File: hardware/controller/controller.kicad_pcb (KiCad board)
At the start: 4 copper layers, 100 x 70 mm, 208 parts, among them J1 USB_C_Receptacle_USB2.0_14P, J10 Conn_01x01, J11 Conn_01x01, J12 Conn_01x09, J13 Mini-SPOX, J14 Mini-SPOX, J2 IDC-10, J3 XT-60, J4 Conn_01x07, J5 Conn_01x01, J6 Conn_01x01, J7 Conn_01x01, J8 Conn_01x09, J9 Conn_01x01, Q1 DMPH4013SK3, Q10 IPD90N04S4L04, Q11 IPD90N04S4L04, Q12 IPD90N04S4L04, Q13 IPD90N04S4L04, Q2 IPD90N04S4L04, Q3 IPD90N04S4L04, Q4 IPD90N04S4L04, Q5 IPD90N04S4L04, Q6 IPD90N04S4L04, Q7 IPD90N04S4L04, Q8 IPD90N04S4L04, Q9 IPD90N04S4L04, SW1 SW_Push, SW2 SW_SPST, U1 USBLC6-2SC6, U10 MCP6541, U11 LM2105D, U12 MCP6541, U13 LM2105D, U14 MCP6541, U15 LM2105D, U16 MCP6541, U17 LM2105D, U18 MCP6541, U19 LM2105D, U2 STM32H523RETx, U20 TXS0101DBV, U21 TXS0101DBV, U3 ESP32-C3-WROOM-02, U4 LM1117MP-3.3, U5 LV14340, U6 MPU-6050, U7 HMC5883L, U8 MCP6541, U9 LM2105D, Y1 8MHz

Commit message: wip
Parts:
- R14, R16: moved to F.Cu
- moved R20 14.7 mm to (156.0, 59.6)
- moved R2 13.4 mm to (108.8, 59.4), turned to -90 degrees
- moved R18 11.8 mm to (192.2, 63.4)
- moved C35 11.5 mm to (191.4, 68.0), turned to -90 degrees
- moved R19 11.2 mm to (192.2, 65.4), turned to 180 degrees
- moved C30 11.0 mm to (182.0, 63.8)
- moved C31 8.32 mm to (186.4, 70.4), turned to 0 degrees
- moved C33 5.74 mm to (175.6, 66.0), turned to 0 degrees
- moved C32 5.47 mm to (176.4, 63.6), turned to 0 degrees
- moved R17 5.47 mm to (170.6, 63.4)
- moved D4 5.47 mm to (170.6, 65.4)
- moved R16 5.34 mm to (160.0, 90.8)
- moved R14 5.26 mm to (163.4, 90.8)
- moved C18 2.76 mm to (158.2, 62.2), turned to 90 degrees
- moved C37 2.30 mm to (152.8, 53.2)
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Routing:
- net SERVO2_DATA: track 4.53 -> 114.6 mm
- net Net-(SW2-A): track 0.00 -> 80.4 mm, vias 0 -> 1
- net +5V: track 15.8 -> 86.2 mm, vias 1 -> 4
- net SERVO1_DATA: track 10.8 -> 63.4 mm
- net GND: track 177.8 -> 213.5 mm, vias 240 -> 258
- net +3.3V: track 163.1 -> 193.4 mm, vias 22 -> 35
- net IMU_SDA: track 28.8 -> 50.7 mm, vias 2 -> 4
- net IMU_SCL: track 29.5 -> 49.5 mm, vias 2 -> 4
- net /microcontroller/STM_RESET: track 16.4 -> 29.7 mm
- net MAG_SCL: track 15.8 -> 26.1 mm
- net IMU_INT: track 24.4 -> 33.1 mm
- net /microcontroller/ESP_USB_CC2: track 6.47 -> 13.2 mm
- net MAG_SDA: track 14.8 -> 21.1 mm
- net /sensors/MAG_C1: track 0.00 -> 6.12 mm
- net Net-(Q1-G): track 0.00 -> 5.65 mm, vias 0 -> 1
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
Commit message: wip - ready, but need double check
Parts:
- moved G*** 85.3 mm to (150.0, 80.7)
- moved G*** 72.5 mm to (145.2, 71.8)
- moved G*** 72.5 mm to (154.2, 71.8)
- moved C73 6.88 mm to (166.5, 109.2), turned to -90 degrees
- moved C69 6.64 mm to (137.5, 109.2), turned to -90 degrees
- moved C70 5.46 mm to (132.8, 105.8), turned to 90 degrees
- moved C74 4.85 mm to (161.0, 106.2), turned to 180 degrees
- moved R15 0.87 mm to (148.0, 89.2), turned to 0 degrees
- moved D4 0.81 mm to (169.8, 65.4)
- moved R17 0.81 mm to (169.8, 63.4)
- moved R14 0.80 mm to (163.4, 91.6)
- moved R16 0.80 mm to (160.0, 91.6)
- moved U20 0.56 mm to (134.0, 109.5), turned to 180 degrees
- moved U21 0.56 mm to (163.0, 109.5), turned to 180 degrees
- moved C72 0.25 mm to (136.8, 109.5)
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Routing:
- net +3.3V: track 193.4 -> 296.3 mm, vias 35 -> 45
- net +5V: track 86.2 -> 164.0 mm, vias 4 -> 7
- net GND: track 213.5 -> 265.9 mm, vias 258 -> 300
- net SERVO1_DATA: track 63.4 -> 88.5 mm
- net VBUS: track 78.5 -> 99.8 mm
- net Net-(U5-FB): track 0.00 -> 11.8 mm, vias 0 -> 1
- net Net-(U5-SS): track 0.00 -> 5.17 mm
- net SERVO2_DATA: track 114.6 -> 109.7 mm
- net Net-(U5-BOOT): track 0.00 -> 3.59 mm
- net Net-(D3-K): track 0.00 -> 3.53 mm
- net /servos/SERVO2_TTL: track 0.00 -> 3.11 mm
- net /servos/SERVO1_TTL: track 0.00 -> 3.11 mm
- net Net-(U5-RT/SYNC): track 0.00 -> 2.41 mm
- net Net-(SW2-A): track 80.4 -> 78.0 mm, vias 1 -> 3
- net /microcontroller/STM_SWDIO: track 26.0 -> 25.3 mm
- added copper zone on B.Cu, net +3.3V
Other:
- board text added: "2"
- board text added: "3V3 LED"
- board text added: "ADC"
- board text added: "BATTERY"
- board text added: "CMP"
- board text added: "DATA"
- board text added: "ESP LED"
- board text added: "ESP USB"
- board text added: "Hogger Controller V1.1 by Eryk Możdżeń March 2025"
- board text added: "MOTOR1"
- board text added: "MOTOR2"
- board text added: "OPTICAL"
- board text added: "PWR"
- board text added: "SERVO1"
- board text added: "SERVO2"
- board text added: "STM LED"
- board text added: "STM RESET"
- board text added: "STM SWD"
- board text added: "U"
- board text added: "UF"
- board text added: "UH"
- board text added: "UL"
- board text added: "V"
- board text added: "VF"
- board text added: "VH"
- board text added: "VL"
- board text added: "W"
- board text added: "WF"
- board text added: "WH"
- board text added: "WL"
- board text removed: "Hogger^2 Controller V1.1 by Eryk Możdżeń March 2025"
- board text removed: "OPTICAL FLOW"
- board text removed: "SWD"
- board text removed: "SWO"

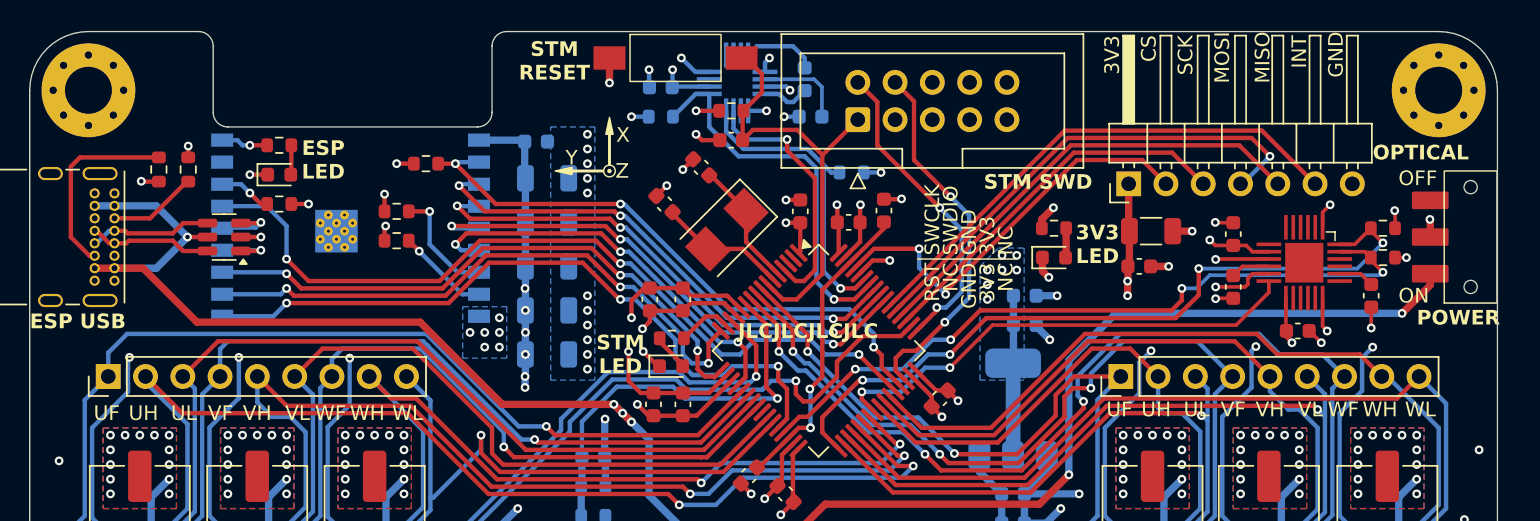
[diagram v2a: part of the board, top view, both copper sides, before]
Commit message: check and fix DRC errors
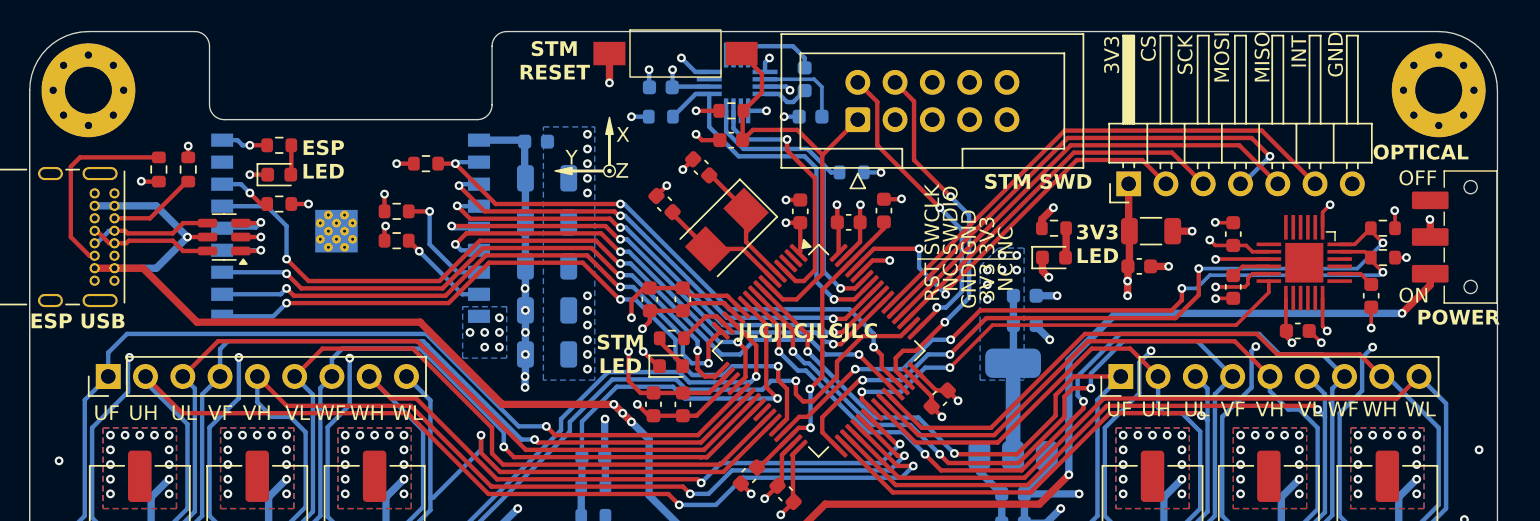
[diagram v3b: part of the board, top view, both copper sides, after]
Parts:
- moved SW1 0.30 mm to (144.0, 51.5)
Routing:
- net unconnected-(J1-SHIELD-PadS1)_1: track 0.00 -> 15.4 mm
- net GND: track 265.9 -> 255.8 mm
- net MOTOR1_PWM_WH: track 73.6 -> 72.3 mm
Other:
- outline, holes or cut-outs redrawn
